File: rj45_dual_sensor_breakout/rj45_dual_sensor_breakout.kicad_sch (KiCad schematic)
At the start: 9 parts, among them J1 RJ45, J2 GND, J3 V, J4 GPIO, J5 RJ45

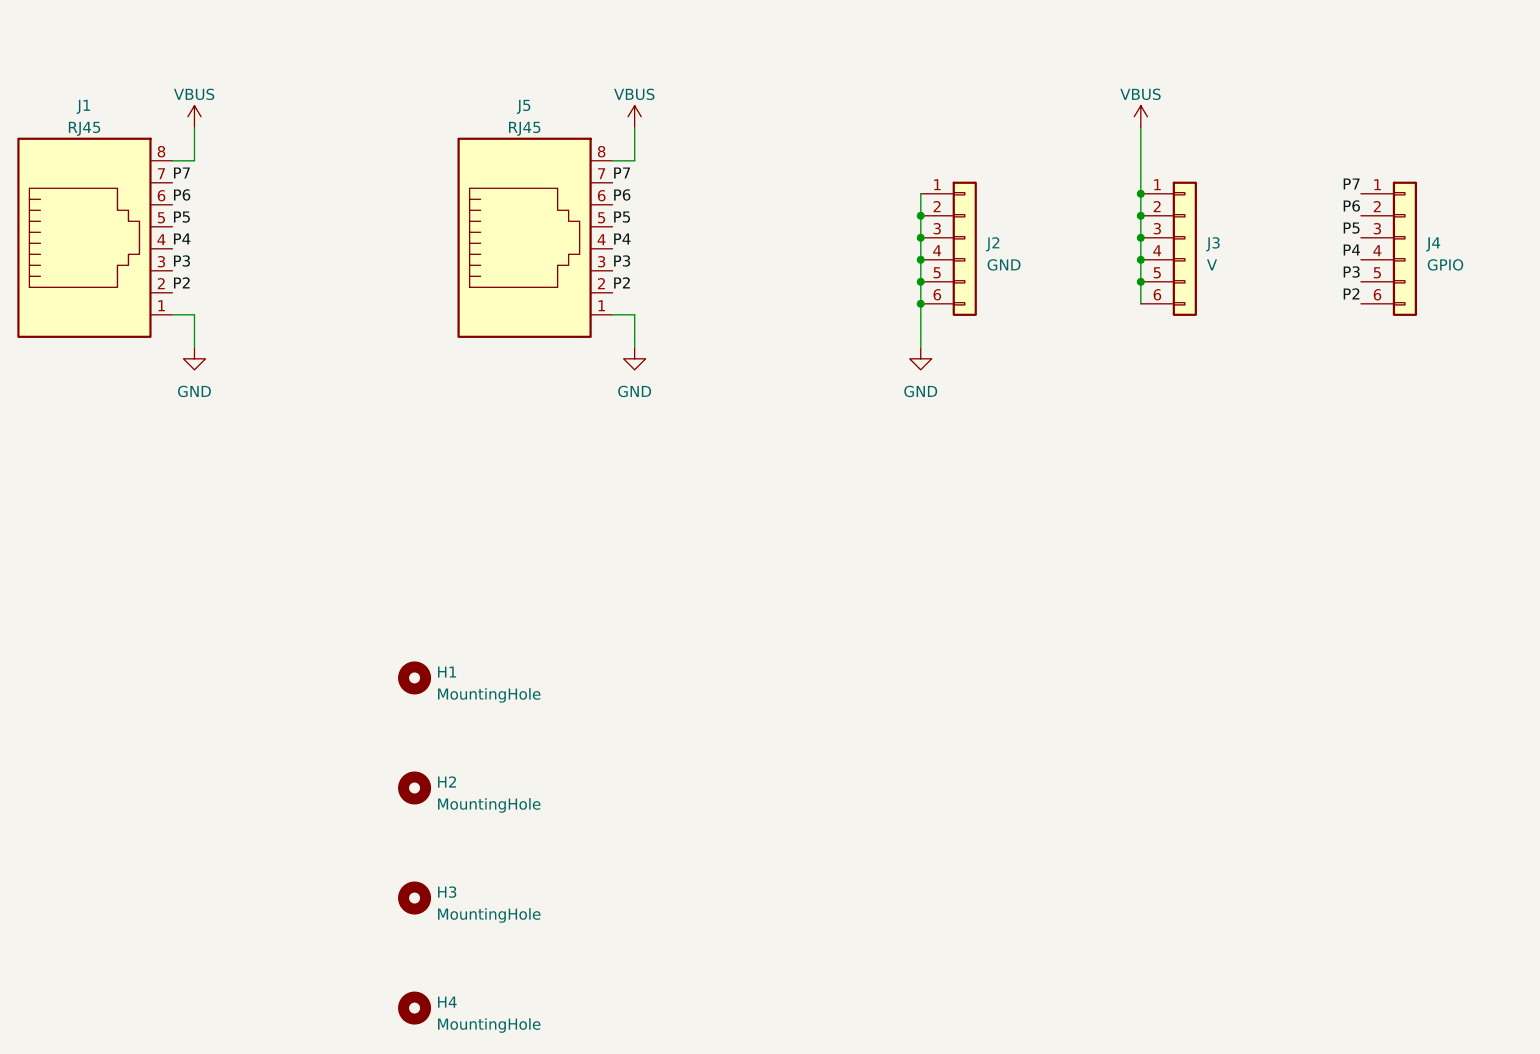
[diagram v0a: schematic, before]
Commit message: RJ45 dual sensor breakout
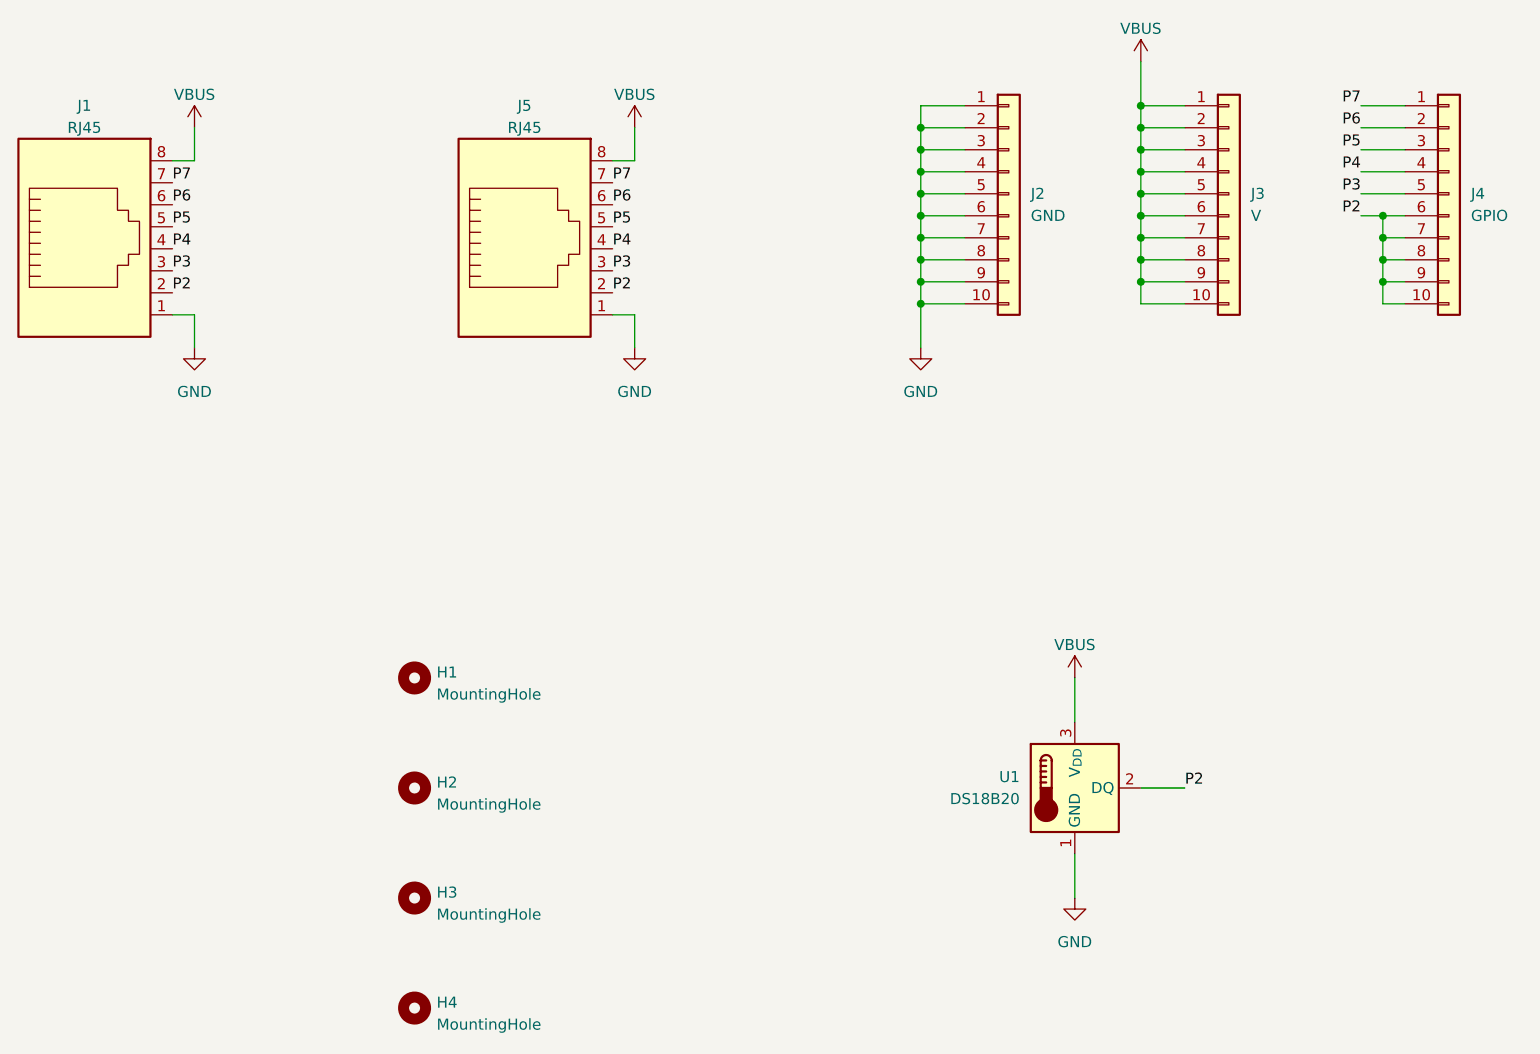
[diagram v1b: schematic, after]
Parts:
- removed J2: GND, Connector_PinHeader_2.54mm:PinHeader_1x06_P2.54mm_Vertical, symbol Connector_Generic:Conn_01x06
- removed J3: V, Connector_PinHeader_2.54mm:PinHeader_1x06_P2.54mm_Vertical, symbol Connector_Generic:Conn_01x06
- removed J4: GPIO, Connector_PinHeader_2.54mm:PinHeader_1x06_P2.54mm_Vertical, symbol Connector_Generic:Conn_01x06
- added J2: GND, Connector_PinHeader_2.54mm:PinHeader_1x10_P2.54mm_Vertical, symbol Connector_Generic:Conn_01x10
- added J3: V, Connector_PinHeader_2.54mm:PinHeader_1x10_P2.54mm_Vertical, symbol Connector_Generic:Conn_01x10
- added J4: GPIO, Connector_PinHeader_2.54mm:PinHeader_1x10_P2.54mm_Vertical, symbol Connector_Generic:Conn_01x10
- added U1: DS18B20, Package_TO_SOT_THT:TO-92_Inline, symbol Sensor_Temperature:DS18B20
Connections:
- net GND: now also J2.1 (Pin_1), J2.10 (Pin_10), J2.2 (Pin_2), J2.3 (Pin_3), J2.4 (Pin_4), J2.5 (Pin_5), J2.6 (Pin_6), J2.7 (Pin_7), J2.8 (Pin_8), J2.9 (Pin_9), U1.1 (GND)
- net P2: now also J4.10 (Pin_10), J4.6 (Pin_6), J4.7 (Pin_7), J4.8 (Pin_8), J4.9 (Pin_9), U1.2 (DQ)
- net P3: now also J4.5 (Pin_5)
- net P4: now also J4.4 (Pin_4)
- net P5: now also J4.3 (Pin_3)
- net P6: now also J4.2 (Pin_2)
- net P7: now also J4.1 (Pin_1)
- net VBUS: now also J3.1 (Pin_1), J3.10 (Pin_10), J3.2 (Pin_2), J3.3 (Pin_3), J3.4 (Pin_4), J3.5 (Pin_5), J3.6 (Pin_6), J3.7 (Pin_7), J3.8 (Pin_8), J3.9 (Pin_9), U1.3 (V_{DD})
